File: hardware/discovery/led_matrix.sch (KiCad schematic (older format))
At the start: 25 parts

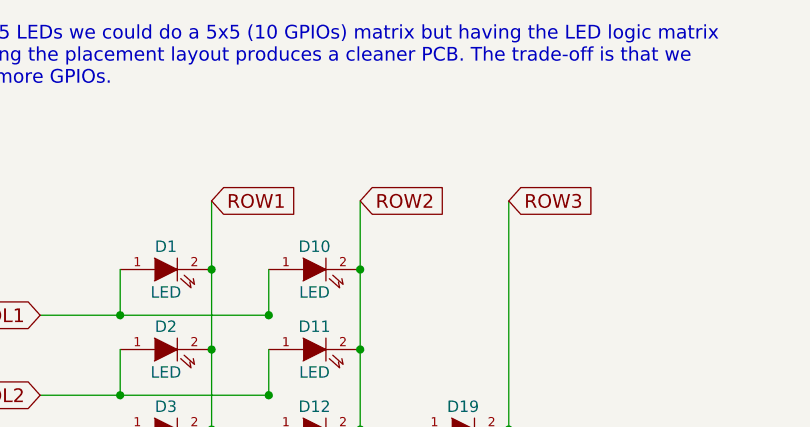
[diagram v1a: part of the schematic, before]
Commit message: Discovery: Fix pull-ups and add LED current limiters
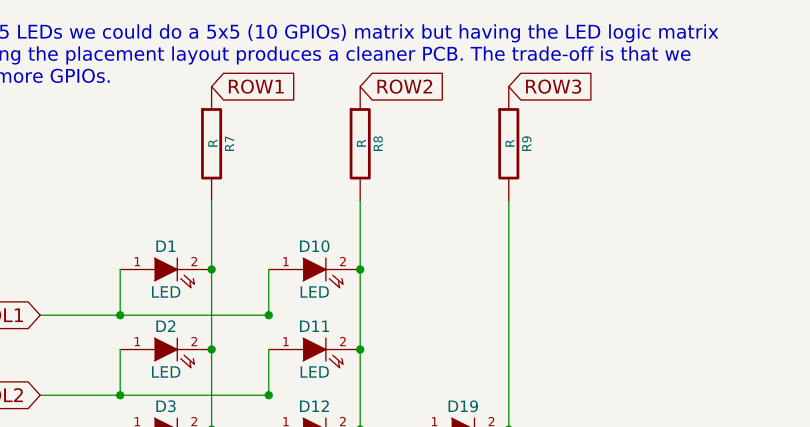
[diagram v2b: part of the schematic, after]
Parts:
- added R7, R8, R9: R, Resistors_SMD:R_0805, symbol R
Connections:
- net ROW1: now also R7.1; no longer D1.2 (K), D2.2 (K), D3.2 (K), D4.2 (K), D5.2 (K), D6.2 (K), D7.2 (K), D8.2 (K), D9.2 (K)
- net ROW2: now also R8.1; no longer D10.2 (K), D11.2 (K), D12.2 (K), D13.2 (K), D14.2 (K), D15.2 (K), D16.2 (K), D17.2 (K), D18.2 (K)
- net ROW3: now also R9.1; no longer D19.2 (K), D20.2 (K), D21.2 (K), D22.2 (K), D23.2 (K), D24.2 (K), D25.2 (K)
- new net: D10.2 (K), D11.2 (K), D12.2 (K), D13.2 (K), D14.2 (K), D15.2 (K), D16.2 (K), D17.2 (K), D18.2 (K), R8.2
- new net: D1.2 (K), D2.2 (K), D3.2 (K), D4.2 (K), D5.2 (K), D6.2 (K), D7.2 (K), D8.2 (K), D9.2 (K), R7.2
- new net: D19.2 (K), D20.2 (K), D21.2 (K), D22.2 (K), D23.2 (K), D24.2 (K), D25.2 (K), R9.2
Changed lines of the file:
@@
 	1    0    0    -1
 $EndComp
-Text GLabel 4350 2250 2    60   Input ~ 0
+Text GLabel 4350 1750 2    60   Input ~ 0
 ROW1
-Text GLabel 5000 2250 2    60   Input ~ 0
+Text GLabel 5000 1750 2    60   Input ~ 0
 ROW2
-Text GLabel 5650 2250 2    60   Input ~ 0
+Text GLabel 5650 1750 2    60   Input ~ 0
 ROW3
 Text GLabel 3600 2750 0    60   Input ~ 0
@@
 Text Notes 3150 1750 0    60   ~ 0
 With 25 LEDs we could do a 5x5 (10 GPIOs) matrix but having the LED logic matrix \nfollowing the placement layout produces a cleaner PCB. The trade-off is that we\nuse 2 more GPIOs.
+$Comp
+L R R7
+U 1 1 5862A3A6
+P 4350 2000
+F 0 "R7" V 4430 2000 40  0000 C CNN
+F 1 "R" V 4357 2001 40  0000 C CNN
+F 2 "Resistors_SMD:R_0805" V 4280 2000 30  0001 C CNN
+F 3 "" H 4350 2000 30  0000 C CNN
+	1    4350 2000
+	1    0    0    -1
+$EndComp
+$Comp
+L R R8
+U 1 1 5862A65F
+P 5000 2000
+F 0 "R8" V 5080 2000 40  0000 C CNN
+F 1 "R" V 5007 2001 40  0000 C CNN
+F 2 "Resistors_SMD:R_0805" V 4930 2000 30  0001 C CNN
+F 3 "" H 5000 2000 30  0000 C CNN
+	1    5000 2000
+	1    0    0    -1
+$EndComp
+$Comp
+L R R9
+U 1 1 5862A6DA
+P 5650 2000
+F 0 "R9" V 5730 2000 40  0000 C CNN
+F 1 "R" V 5657 2001 40  0000 C CNN
+F 2 "Resistors_SMD:R_0805" V 5580 2000 30  0001 C CNN
+F 3 "" H 5650 2000 30  0000 C CNN
+	1    5650 2000
+	1    0    0    -1
+$EndComp
 $EndSCHEMATC

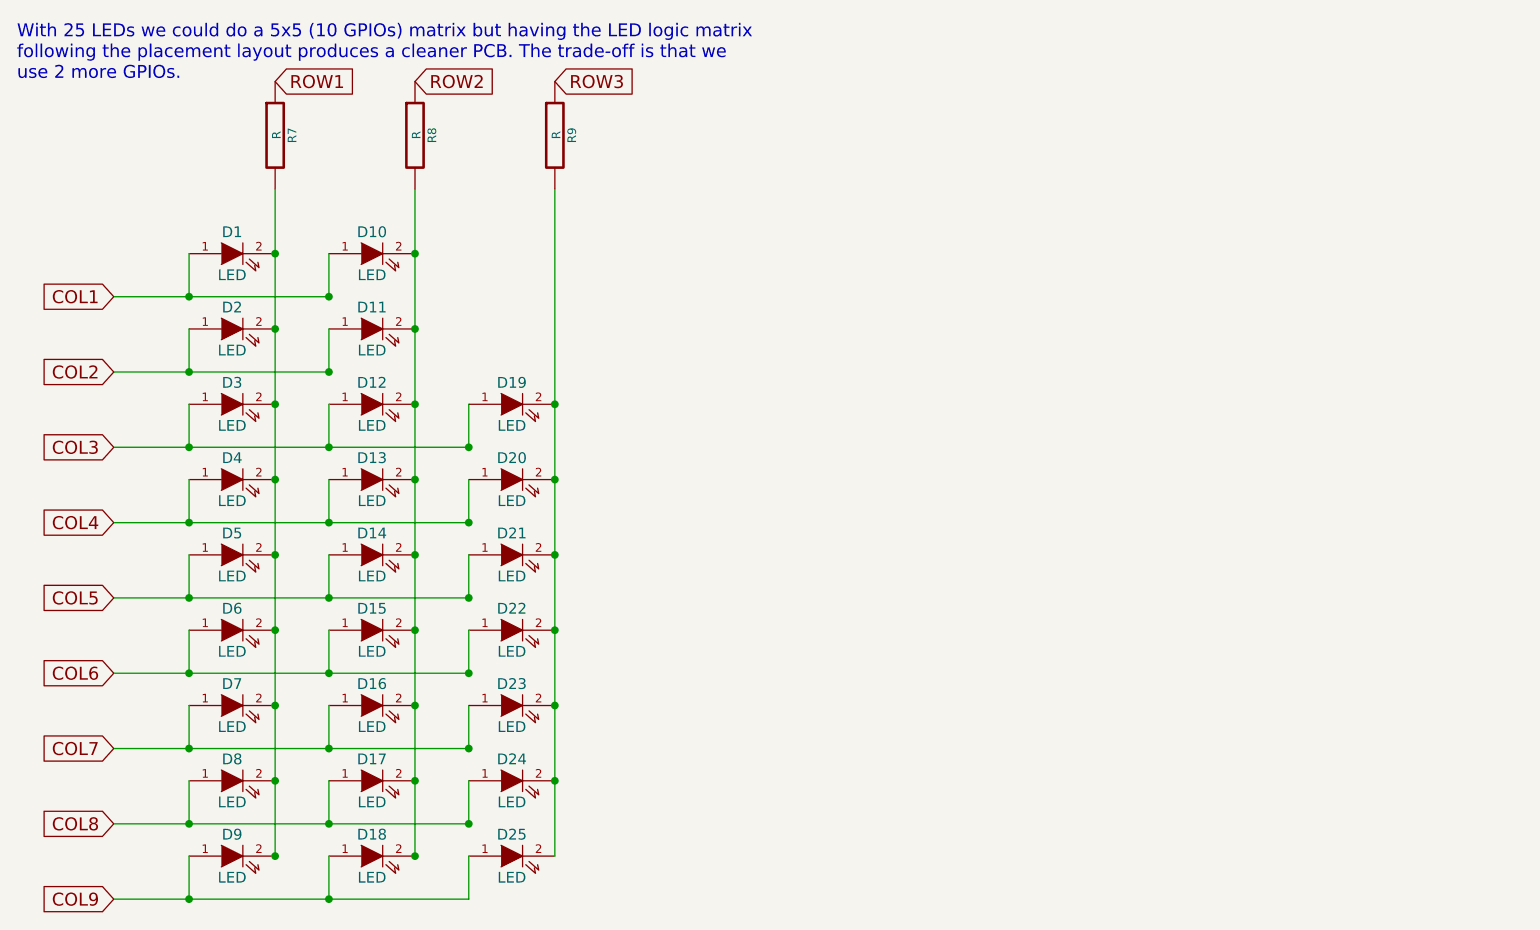
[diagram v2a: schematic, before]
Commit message: Discovery: Add OLED screen
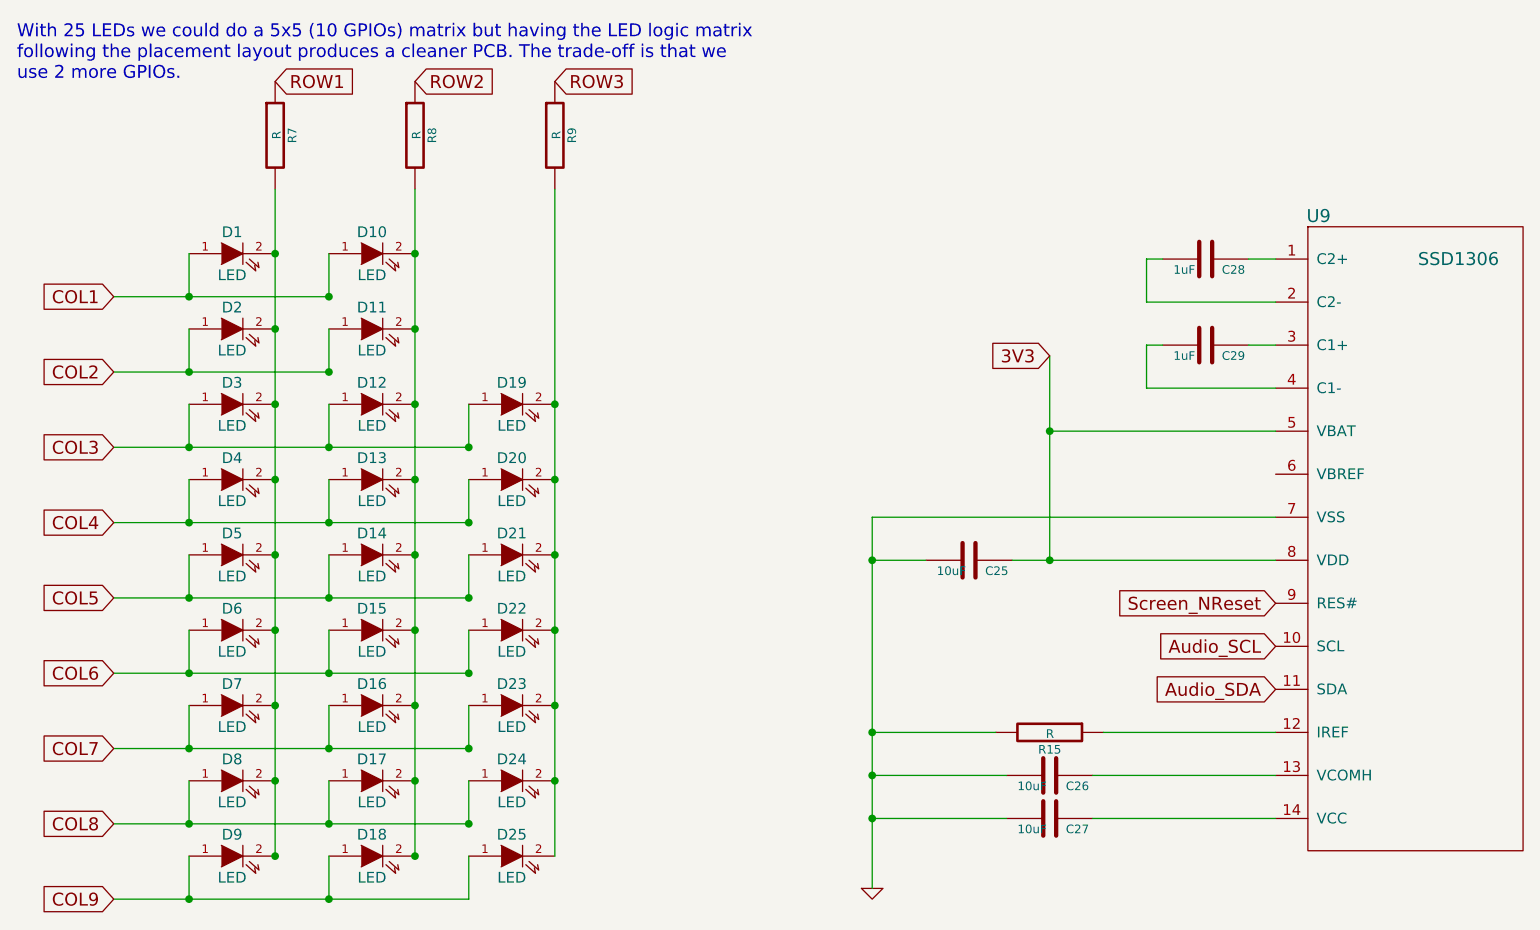
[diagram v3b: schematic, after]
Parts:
- added C25, C26, C27: 10uF, Capacitors_SMD:C_0805, symbol C
- added C28, C29: 1uF, Capacitors_SMD:C_0805, symbol C
- added R15: R, Resistors_SMD:R_0805, symbol R
- added U9: SSD1306, stm32f4-disco:MIDAS_MCOT096016AV_OLED, symbol SSD1306
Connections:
- new net: C28.1, U9.1 (C2+)
- new net: R15.1, U9.12 (IREF)
- new net: C26.1, U9.13 (VCOMH)
- new net: C27.1, U9.14 (VCC)
- new net: C28.2, U9.2 (C2-)
- new net: C29.1, U9.3 (C1+)
- new net: C29.2, U9.4 (C1-)
- new net 3V3: C25.1, U9.5 (VBAT), U9.8 (VDD)
- new net Audio_SCL: U9.10 (SCL)
- new net Audio_SDA: U9.11 (SDA)
- new net GND: C25.2, C26.2, C27.2, R15.2, U9.7 (VSS)
- new net Screen_NReset: U9.9 (RES#)
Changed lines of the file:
@@
 Text GLabel 3600 5550 0    60   Input ~ 0
 COL9
+Text Notes 3150 1750 0    60   ~ 0
+With 25 LEDs we could do a 5x5 (10 GPIOs) matrix but having the LED logic matrix \nfollowing the placement layout produces a cleaner PCB. The trade-off is that we\nuse 2 more GPIOs.
+$Comp
+L R R7
+U 1 1 5862A3A6
+P 4350 2000
+F 0 "R7" V 4430 2000 40  0000 C CNN
+F 1 "R" V 4357 2001 40  0000 C CNN
+F 2 "Resistors_SMD:R_0805" V 4280 2000 30  0001 C CNN
+F 3 "" H 4350 2000 30  0000 C CNN
+	1    4350 2000
+	1    0    0    -1
+$EndComp
+$Comp
+L R R8
+U 1 1 5862A65F
+P 5000 2000
+F 0 "R8" V 5080 2000 40  0000 C CNN
+F 1 "R" V 5007 2001 40  0000 C CNN
+F 2 "Resistors_SMD:R_0805" V 4930 2000 30  0001 C CNN
+F 3 "" H 5000 2000 30  0000 C CNN
+	1    5000 2000
+	1    0    0    -1
+$EndComp
+$Comp
+L R R9
+U 1 1 5862A6DA
+P 5650 2000
+F 0 "R9" V 5730 2000 40  0000 C CNN
+F 1 "R" V 5657 2001 40  0000 C CNN
+F 2 "Resistors_SMD:R_0805" V 5580 2000 30  0001 C CNN
+F 3 "" H 5650 2000 30  0000 C CNN
+	1    5650 2000
+	1    0    0    -1
+$EndComp
+$Comp
+L SSD1306 U9
+U 1 1 58642D78
+P 9200 2375
+F 0 "U9" H 9200 2375 60  0000 C CNN
+F 1 "SSD1306" H 9850 2175 60  0000 C CNN
+F 2 "stm32f4-disco:MIDAS_MCOT096016AV_OLED" H 9200 2375 60  0001 C CNN
+F 3 "" H 9200 2375 60  0001 C CNN
+	1    9200 2375
+	1    0    0    -1
+$EndComp
+$Comp
+L C C28
+U 1 1 586433AA
+P 8675 2575
+F 0 "C28" V 8725 2650 40  0000 L CNN
+F 1 "1uF" V 8725 2425 40  0000 L CNN
+F 2 "Capacitors_SMD:C_0805" H 8713 2425 30  0001 C CNN
+F 3 "" H 8675 2575 60  0000 C CNN
+	1    8675 2575
+	0    1    1    0
+$EndComp
+$Comp
+L C C29
+U 1 1 58643880
+P 8675 2975
+F 0 "C29" V 8725 3050 40  0000 L CNN
+F 1 "1uF" V 8725 2825 40  0000 L CNN
+F 2 "Capacitors_SMD:C_0805" H 8713 2825 30  0001 C CNN
+F 3 "" H 8675 2975 60  0000 C CNN
+	1    8675 2975
+	0    1    1    0
+$EndComp
+Text GLabel 7950 3025 0    60   Input ~ 0
+3V3
+Text GLabel 9000 4175 0    60   Input ~ 0
+Screen_NReset
+Text GLabel 9000 4375 0    60   Input ~ 0
+Audio_SCL
+Text GLabel 9000 4575 0    60   Input ~ 0
+Audio_SDA
 Connection ~ 4350 2900
 Connection ~ 4350 3250
@@
 Wire Wire Line
 	3600 3100 4600 3100
-Text Notes 3150 1750 0    60   ~ 0
-With 25 LEDs we could do a 5x5 (10 GPIOs) matrix but having the LED logic matrix \nfollowing the placement layout produces a cleaner PCB. The trade-off is that we\nuse 2 more GPIOs.
-$Comp
-L R R7
-U 1 1 5862A3A6
-P 4350 2000
-F 0 "R7" V 4430 2000 40  0000 C CNN
-F 1 "R" V 4357 2001 40  0000 C CNN
-F 2 "Resistors_SMD:R_0805" V 4280 2000 30  0001 C CNN
-F 3 "" H 4350 2000 30  0000 C CNN
-	1    4350 2000
-	1    0    0    -1
-$EndComp
-$Comp
-L R R8
-U 1 1 5862A65F
-P 5000 2000
-F 0 "R8" V 5080 2000 40  0000 C CNN
-F 1 "R" V 5007 2001 40  0000 C CNN
-F 2 "Resistors_SMD:R_0805" V 4930 2000 30  0001 C CNN
-F 3 "" H 5000 2000 30  0000 C CNN
-	1    5000 2000
-	1    0    0    -1
-$EndComp
-$Comp
-L R R9
-U 1 1 5862A6DA
-P 5650 2000
-F 0 "R9" V 5730 2000 40  0000 C CNN
-F 1 "R" V 5657 2001 40  0000 C CNN
-F 2 "Resistors_SMD:R_0805" V 5580 2000 30  0001 C CNN
-F 3 "" H 5650 2000 30  0000 C CNN
-	1    5650 2000
-	1    0    0    -1
-$EndComp
+Wire Wire Line
+	9000 2575 8875 2575
+Wire Wire Line
+	8475 2575 8400 2575
+Wire Wire Line
+	8400 2575 8400 2775
+Wire Wire Line
+	8400 2775 9000 2775
+Wire Wire Line
+	9000 2975 8875 2975
+Wire Wire Line
+	8475 2975 8400 2975
+Wire Wire Line
+	8400 2975 8400 3175
+Wire Wire Line
+	8400 3175 9000 3175
+Wire Wire Line
+	9000 3375 7950 3375
+Wire Wire Line
+	7950 3025 7950 3975
+Connection ~ 7950 3375
+Wire Wire Line
+	7775 3975 9000 3975
+Wire Wire Line
+	9000 3775 7125 3775
+Wire Wire Line
+	7125 3775 7125 5500
+$Comp
+L C C25
+U 1 1 586463AC
+P 7575 3975
+F 0 "C25" V 7625 4050 40  0000 L CNN
+F 1 "10uF" V 7625 3825 40  0000 L CNN
+F 2 "Capacitors_SMD:C_0805" H 7613 3825 30  0001 C CNN
+F 3 "" H 7575 3975 60  0000 C CNN
+	1    7575 3975
+	0    1    1    0
+$EndComp
+Connection ~ 7950 3975
+Wire Wire Line
+	7375 3975 7125 3975
+Connection ~ 7125 3975
+$Comp
+L GND #PWR025
+U 1 1 586468A3
+P 7125 5500
+F 0 "#PWR025" H 7125 5500 30  0001 C CNN
+F 1 "GND" H 7125 5430 30  0001 C CNN
+F 2 "" H 7125 5500 60  0001 C CNN
+F 3 "" H 7125 5500 60  0001 C CNN
+	1    7125 5500
+	1    0    0    -1
+$EndComp
+$Comp
+L R R15
+U 1 1 58646E77
+P 7950 4775
+F 0 "R15" V 8030 4775 40  0000 C CNN
+F 1 "R" V 7957 4776 40  0000 C CNN
+F 2 "Resistors_SMD:R_0805" V 7880 4775 30  0001 C CNN
+F 3 "" H 7950 4775 30  0000 C CNN
+	1    7950 4775
+	0    1    1    0
+$EndComp
+$Comp
+L C C26
+U 1 1 58646F61
+P 7950 4975
+F 0 "C26" V 8000 5050 40  0000 L CNN
+F 1 "10uF" V 8000 4825 40  0000 L CNN
+F 2 "Capacitors_SMD:C_0805" H 7988 4825 30  0001 C CNN
+F 3 "" H 7950 4975 60  0000 C CNN
+	1    7950 4975
+	0    1    1    0
+$EndComp
+$Comp
+L C C27
+U 1 1 58647031
+P 7950 5175
+F 0 "C27" V 8000 5250 40  0000 L CNN
+F 1 "10uF" V 8000 5025 40  0000 L CNN
+F 2 "Capacitors_SMD:C_0805" H 7988 5025 30  0001 C CNN
+F 3 "" H 7950 5175 60  0000 C CNN
+	1    7950 5175
+	0    1    1    0
+$EndComp
+Wire Wire Line
+	9000 4775 8200 4775
+Wire Wire Line
+	7700 4775 7125 4775
+Connection ~ 7125 4775
+Wire Wire Line
+	9000 4975 8150 4975
+Wire Wire Line
+	7750 4975 7125 4975
+Connection ~ 7125 4975
+Wire Wire Line
+	9000 5175 8150 5175
+Wire Wire Line
+	7750 5175 7125 5175
+Connection ~ 7125 5175
 $EndSCHEMATC

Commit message: Discovery: Add two encoders and remove the BPM button
BPM and volume will be changed with a long press of the play button and
the encoders
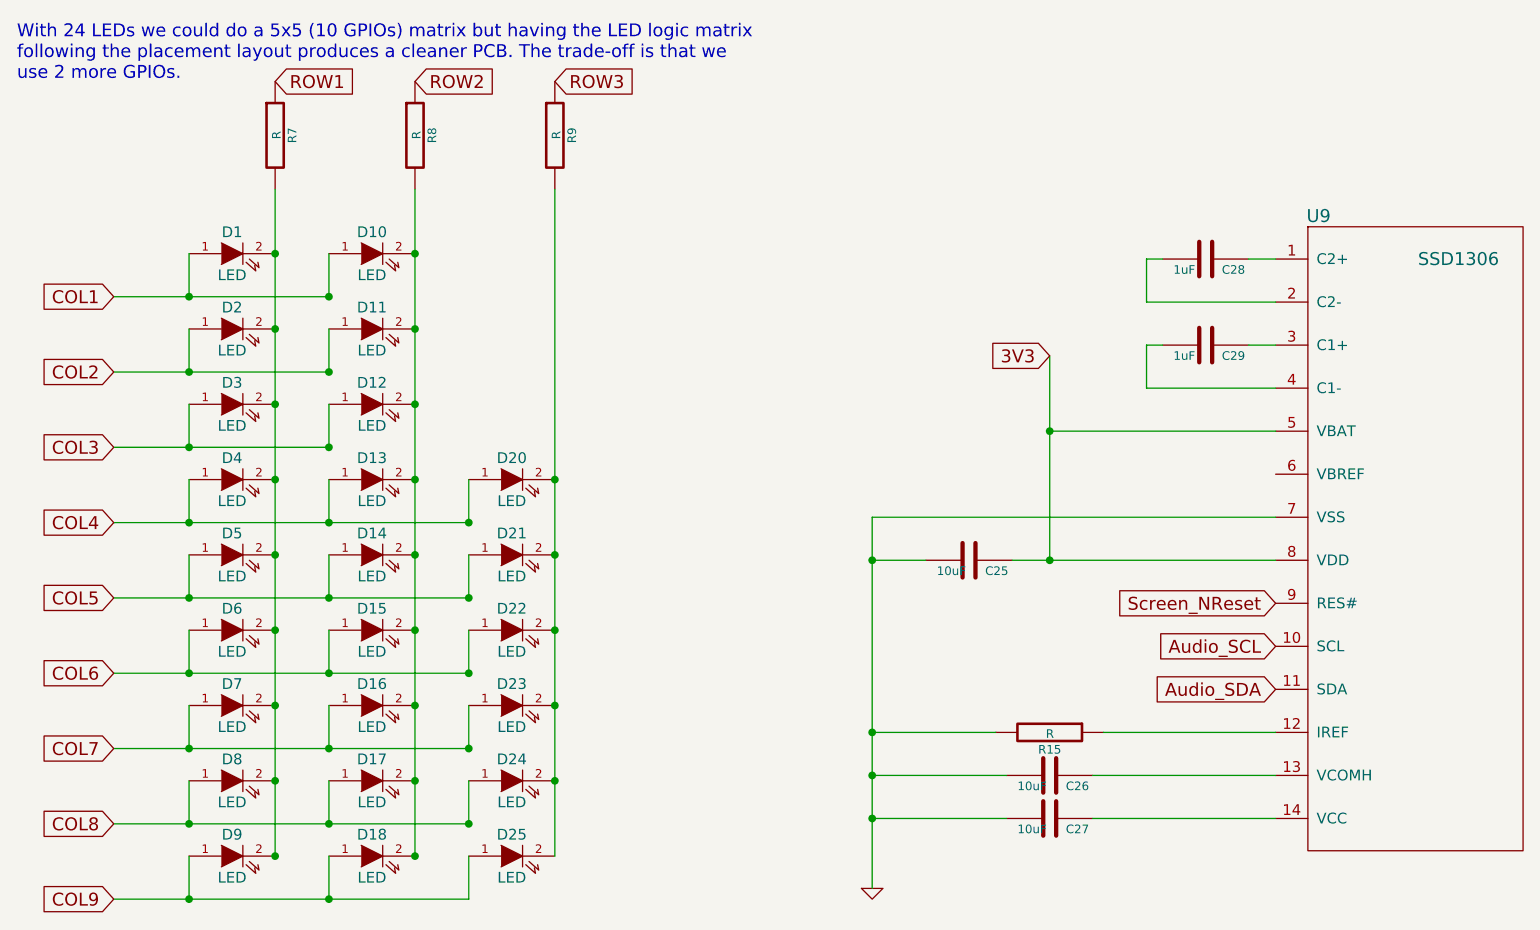
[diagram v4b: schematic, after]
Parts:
- removed D19: LED, LEDs:LED_0805, symbol LED
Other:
- note added: "With 24 LEDs we could do a 5x5 (10 GPIOs) matrix but having the LED logic matrix \nfollowing the placement layout produces a cleaner PCB. The trade-off is that we\nuse 2 more GPIOs."
- note removed: "With 25 LEDs we could do a 5x5 (10 GPIOs) matrix but having the LED logic matrix \nfollowing the placement layout produces a cleaner PCB. The trade-off is that we\nuse 2 more GPIOs."
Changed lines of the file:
@@
-$EndComp
-$Comp
-L LED D19
-U 1 1 585D8AD7
-P 5450 3250
-F 0 "D19" H 5450 3350 50  0000 C CNN
-F 1 "LED" H 5450 3150 50  0000 C CNN
-F 2 "LEDs:LED_0805" H 5450 3250 50  0001 C CNN
-F 3 "" H 5450 3250 50  0000 C CNN
-	1    5450 3250
-	1    0    0    -1
 $EndComp
 $Comp
@@
 COL9
 Text Notes 3150 1750 0    60   ~ 0
-With 25 LEDs we could do a 5x5 (10 GPIOs) matrix but having the LED logic matrix \nfollowing the placement layout produces a cleaner PCB. The trade-off is that we\nuse 2 more GPIOs.
+With 24 LEDs we could do a 5x5 (10 GPIOs) matrix but having the LED logic matrix \nfollowing the placement layout produces a cleaner PCB. The trade-off is that we\nuse 2 more GPIOs.
 $Comp
 L R R7
@@
 Connection ~ 4600 2750
 Wire Wire Line
-	5250 3450 5250 3250
-Connection ~ 5250 3450
-Wire Wire Line
 	4600 4850 4600 4650
 Wire Wire Line
@@
 Connection ~ 4350 4300
 Connection ~ 5000 4300
-Connection ~ 5650 3250
 Connection ~ 5000 2550
 Connection ~ 4350 2550
@@
 Wire Wire Line
 	5250 5550 5250 5350
-Wire Wire Line
-	3600 3450 5250 3450
 Wire Wire Line
 	5250 3800 3600 3800
@@
 Connection ~ 7125 3975
 $Comp
-L GND #PWR025
+L GND #PWR027
 U 1 1 586468A3
 P 7125 5500
-F 0 "#PWR025" H 7125 5500 30  0001 C CNN
+F 0 "#PWR027" H 7125 5500 30  0001 C CNN
 F 1 "GND" H 7125 5430 30  0001 C CNN
 F 2 "" H 7125 5500 60  0001 C CNN
@@
 	7750 5175 7125 5175
 Connection ~ 7125 5175
+Wire Wire Line
+	3600 3450 4600 3450
 $EndSCHEMATC
